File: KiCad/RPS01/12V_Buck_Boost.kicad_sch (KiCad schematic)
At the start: 0 parts

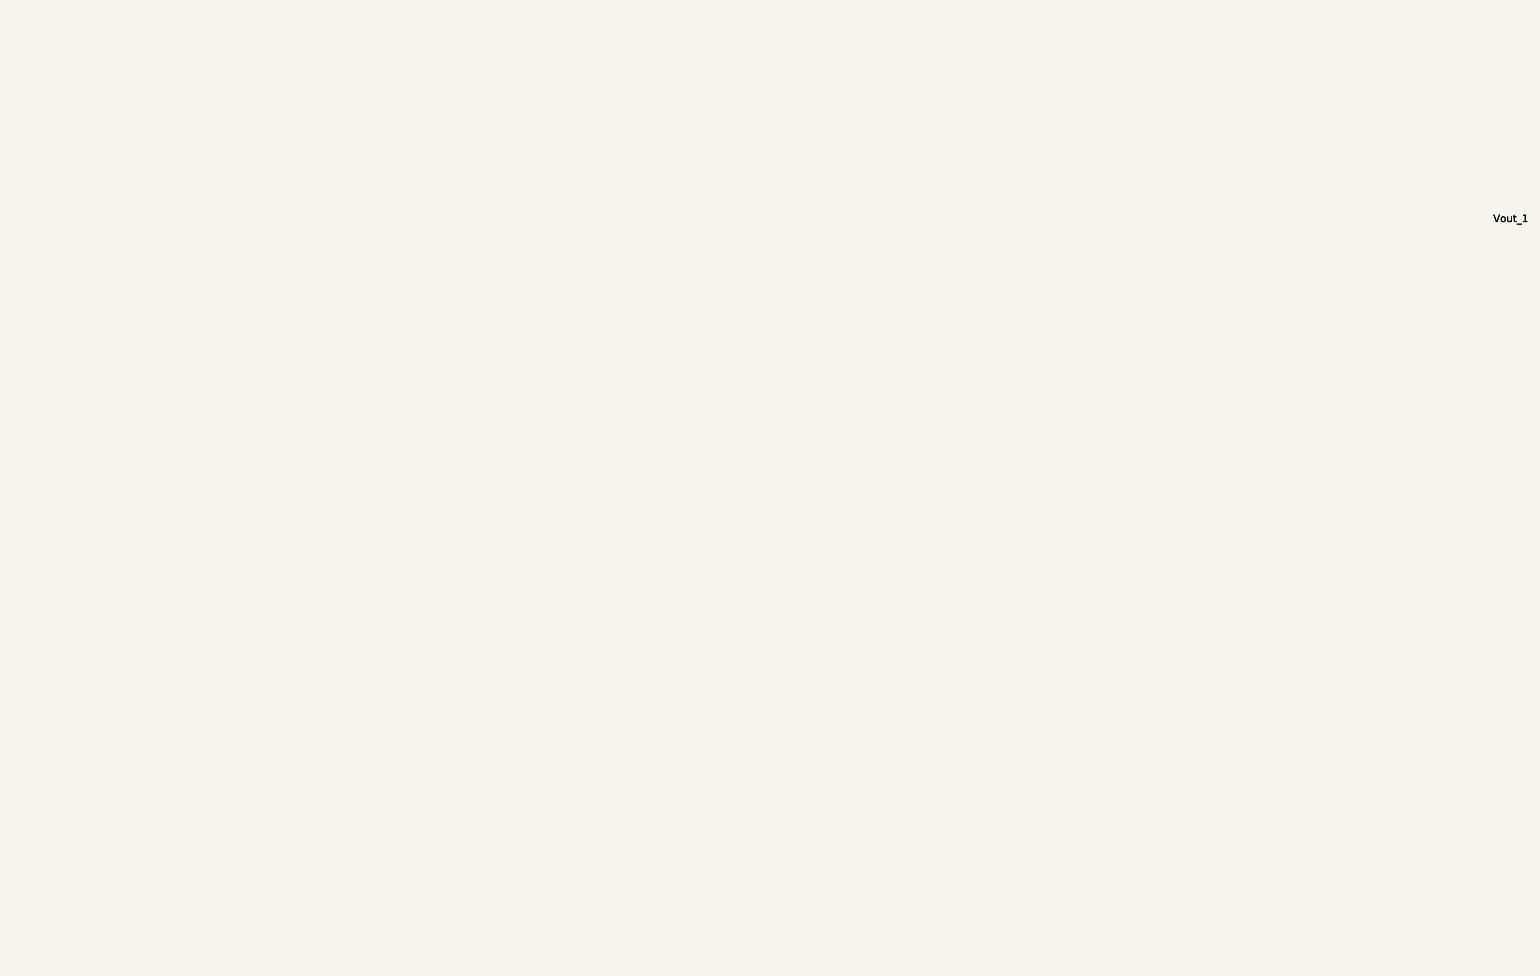
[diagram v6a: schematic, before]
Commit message: Added repaired 12 and 5v
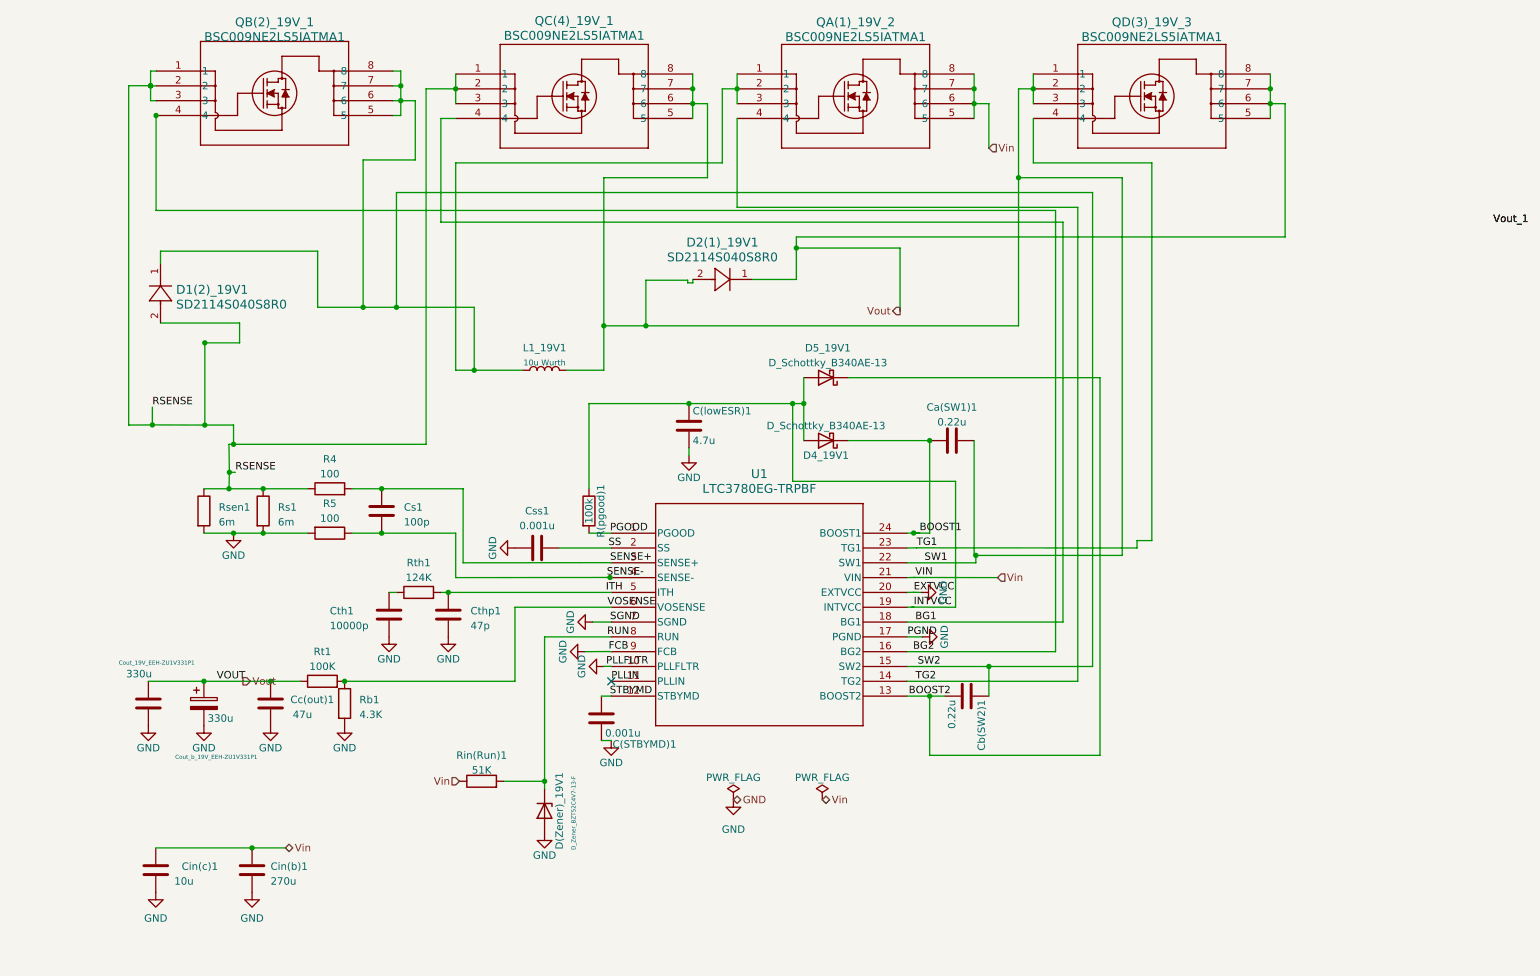
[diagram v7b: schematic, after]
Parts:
- added C(STBYMD)1, Css1: 0.001u, Capacitor_SMD:C_1206_3216Metric, symbol Device:C
- added C(lowESR)1: 4.7u, Mechatronics Cesr:CAPMP7.6X4.3_3.1N_KEM, symbol Device:C
- added Ca(SW1)1, Cb(SW2)1: 0.22u, Capacitor_SMD:C_1206_3216Metric, symbol Device:C
- added Cc(out)1: 47u, Capacitor_SMD:C_1206_3216Metric, symbol Device:C
- added Cin(b)1: 270u, Mechatronic Footprints:LargeCAPSCAPPRD350W60D800H1200, symbol Device:C
- added Cin(c)1: 10u, Capacitor_SMD:C_1206_3216Metric, symbol Device:C
- added Cout_19V_EEH-ZU1V331P1: 330u, Mechatronic Footprints:LargeCAPSCAPPRD350W60D800H1200, symbol Device:C
- added Cout_b_19V_EEH-ZU1V331P1: 330u, Mechatronic Footprints:LargeCAPSCAPPRD350W60D800H1200, symbol Device:C_Polarized
- added Cs1: 100p, Capacitor_SMD:C_1206_3216Metric, symbol Device:C
- added Cth1: 10000p, Capacitor_SMD:C_1206_3216Metric, symbol Device:C
- added Cthp1: 47p, Capacitor_SMD:C_1206_3216Metric, symbol Device:C
- added D(Zener)_19V1: D_Zener_BZT52C4V7-13-F, Mechatronic Footprints:SOD123_DIO, symbol Device:D_Zener
- added D1(2)_19V1, D2(1)_19V1: SD2114S040S8R0, Mechatronics Sdiode:SD2114_AVX, symbol Mechatronics Sdiode:SD2114S040S8R0
- added D4_19V1, D5_19V1: D_Schottky_B340AE-13, Mechatronic Footprints:CR_SMA_320-340AE_DIO, symbol Device:D_Schottky
- added L1_19V1: 10u Wurth, Mechatronic Footprints:IND_410680_WRE, symbol Device:L
- added QA(1)_19V_2, QB(2)_19V_1, QC(4)_19V_1, QD(3)_19V_3: BSC009NE2LS5IATMA1, Mechatronic Footprints:PG-TDSON-8_INF_modified_ken, symbol Mechatronics NMOS:BSC009NE2LS5IATMA1
- added R(pgood)1: 100k, LED_SMD:LED_1206_3216Metric, symbol Device:R
- added R4, R5: 100, Resistor_SMD:R_1206_3216Metric, symbol Device:R
- added Rb1: 4.3K, Resistor_SMD:R_1206_3216Metric, symbol Device:R
- added Rin(Run)1: 51K, Resistor_SMD:R_1206_3216Metric, symbol Device:R
- added Rs1, Rsen1: 6m, Resistor_SMD:R_2512_6332Metric, symbol Device:R
- added Rt1: 100K, Resistor_SMD:R_1206_3216Metric, symbol Device:R
- added Rth1: 124K, Resistor_SMD:R_1206_3216Metric, symbol Device:R
- added U1: LTC3780EG-TRPBF, Mechatronic Footprints:LTC3780_SSOP-24_G_LIT, symbol LTC3780-24-SSOP:LTC3780EG-TRPBF
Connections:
- new net: Cth1.1, Rth1.1
- new net BG1: QC(4)_19V_1.4, U1.18 (BG1)
- new net BG2: QB(2)_19V_1.4, U1.16 (BG2)
- new net BOOST1: Ca(SW1)1.1, D4_19V1.1 (K), U1.24 (BOOST1)
- new net BOOST2: Cb(SW2)1.2, D5_19V1.1 (K), U1.13 (BOOST2)
- new net GND: C(STBYMD)1.2, C(lowESR)1.2, Cc(out)1.2, Cin(b)1.2, Cin(c)1.2, Cout_19V_EEH-ZU1V331P1.2, Cout_b_19V_EEH-ZU1V331P1.2, Css1.1, Cth1.2, Cthp1.2, D(Zener)_19V1.2 (A), R5.2, Rb1.2, Rs1.2, Rsen1.2, U1.10 (PLLFLTR), U1.17 (PGND), U1.20 (EXTVCC), U1.7 (SGND), U1.9 (FCB)
- new net INTVCC: C(lowESR)1.1, D4_19V1.2 (A), D5_19V1.2 (A), R(pgood)1.1, U1.19 (INTVCC)
- new net ITH: Cthp1.1, Rth1.2, U1.5 (ITH)
- new net PGOOD: R(pgood)1.2, U1.1 (PGOOD)
- new net PLLIN: U1.11 (PLLIN)
- new net RSENSE: D1(2)_19V1.2, QB(2)_19V_1.1, QB(2)_19V_1.2, QB(2)_19V_1.3, QC(4)_19V_1.1, QC(4)_19V_1.2, QC(4)_19V_1.3, R4.1, Rs1.1, Rsen1.1
- new net RUN: D(Zener)_19V1.1 (K), Rin(Run)1.2, U1.8 (RUN)
- new net SENSE+: Cs1.2, R4.2, U1.3 (SENSE+)
- new net SENSE-: Cs1.1, R5.1, U1.4 (SENSE-)
- new net SS: Css1.2, U1.2 (SS)
- new net STBYMD: C(STBYMD)1.1, U1.12 (STBYMD)
- new net SW1: Ca(SW1)1.2, D2(1)_19V1.2, L1_19V1.2, QC(4)_19V_1.5, QC(4)_19V_1.6, QC(4)_19V_1.7, QC(4)_19V_1.8, QD(3)_19V_3.1, QD(3)_19V_3.2, QD(3)_19V_3.3, U1.22 (SW1)
- new net SW2: Cb(SW2)1.1, D1(2)_19V1.1, L1_19V1.1, QA(1)_19V_2.1, QA(1)_19V_2.2, QA(1)_19V_2.3, QB(2)_19V_1.5, QB(2)_19V_1.6, QB(2)_19V_1.7, QB(2)_19V_1.8, U1.15 (SW2)
- new net TG1: QD(3)_19V_3.4, U1.23 (TG1)
- new net TG2: QA(1)_19V_2.4, U1.14 (TG2)
- new net VOSENSE: Rb1.1, Rt1.2, U1.6 (VOSENSE)
- new net Vin: Cin(b)1.1, Cin(c)1.1, QA(1)_19V_2.5, QA(1)_19V_2.6, QA(1)_19V_2.7, QA(1)_19V_2.8, Rin(Run)1.1, U1.21 (VIN)
- new net Vout: Cc(out)1.1, Cout_19V_EEH-ZU1V331P1.1, Cout_b_19V_EEH-ZU1V331P1.1, D2(1)_19V1.1, QD(3)_19V_3.5, QD(3)_19V_3.6, QD(3)_19V_3.7, QD(3)_19V_3.8, Rt1.1
- no-connect marks 0 -> 1
